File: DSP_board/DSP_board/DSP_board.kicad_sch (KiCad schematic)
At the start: 62 parts

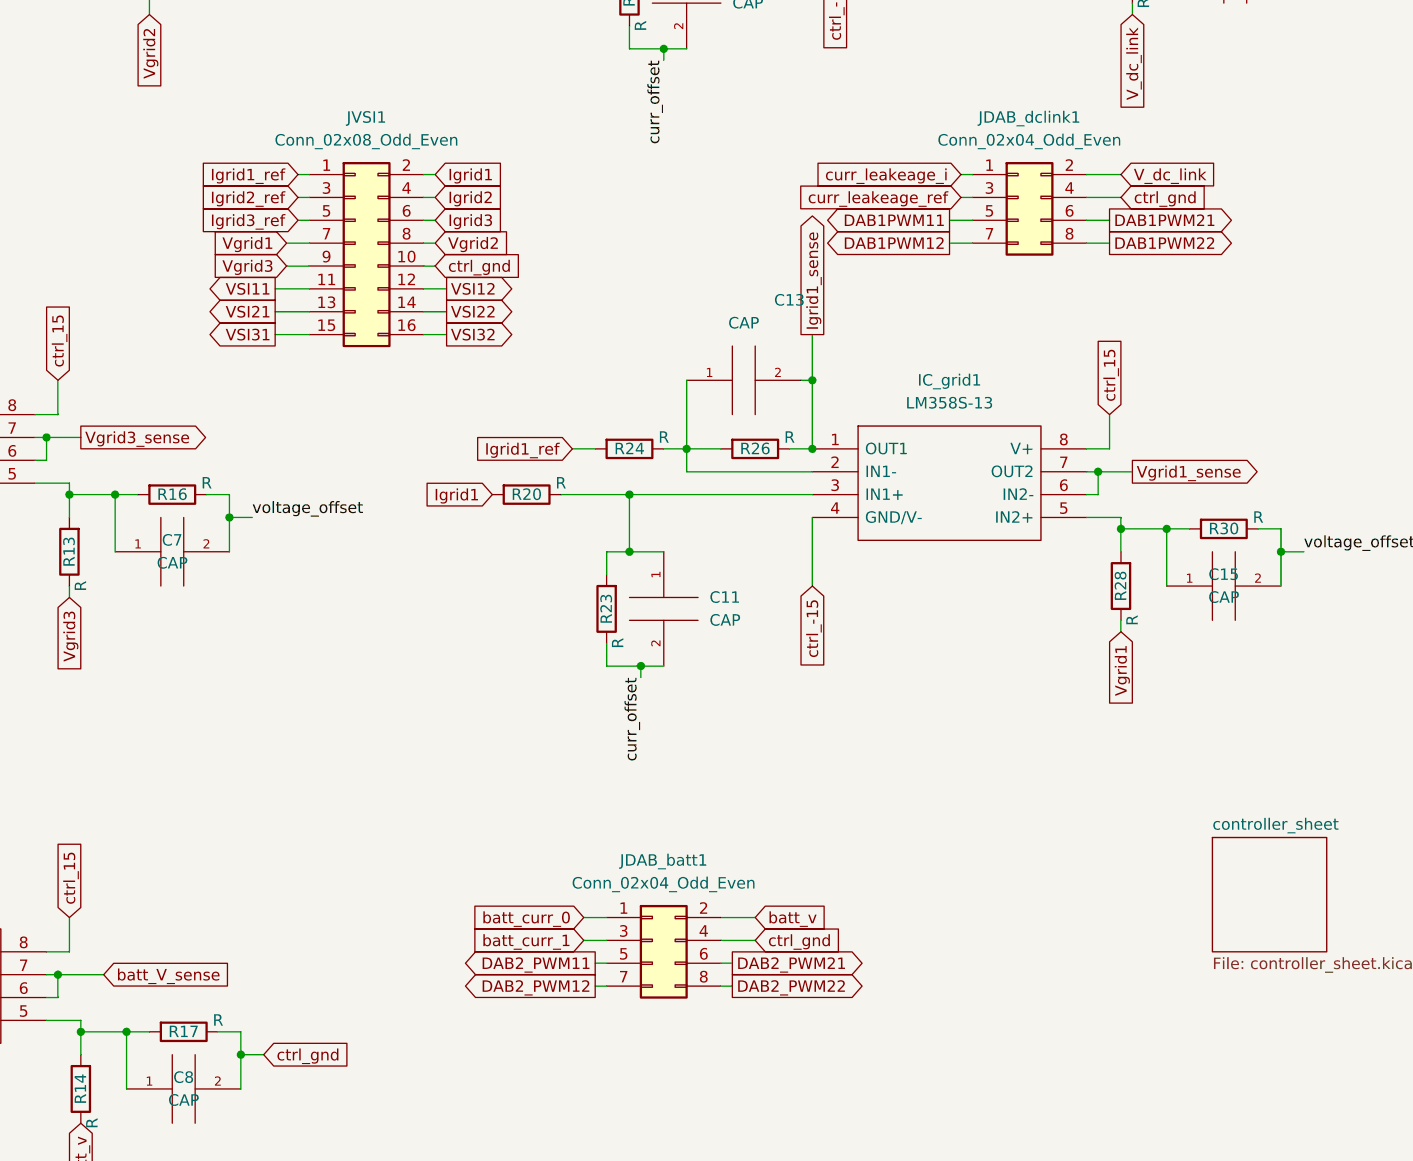
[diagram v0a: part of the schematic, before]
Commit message: including FPGA
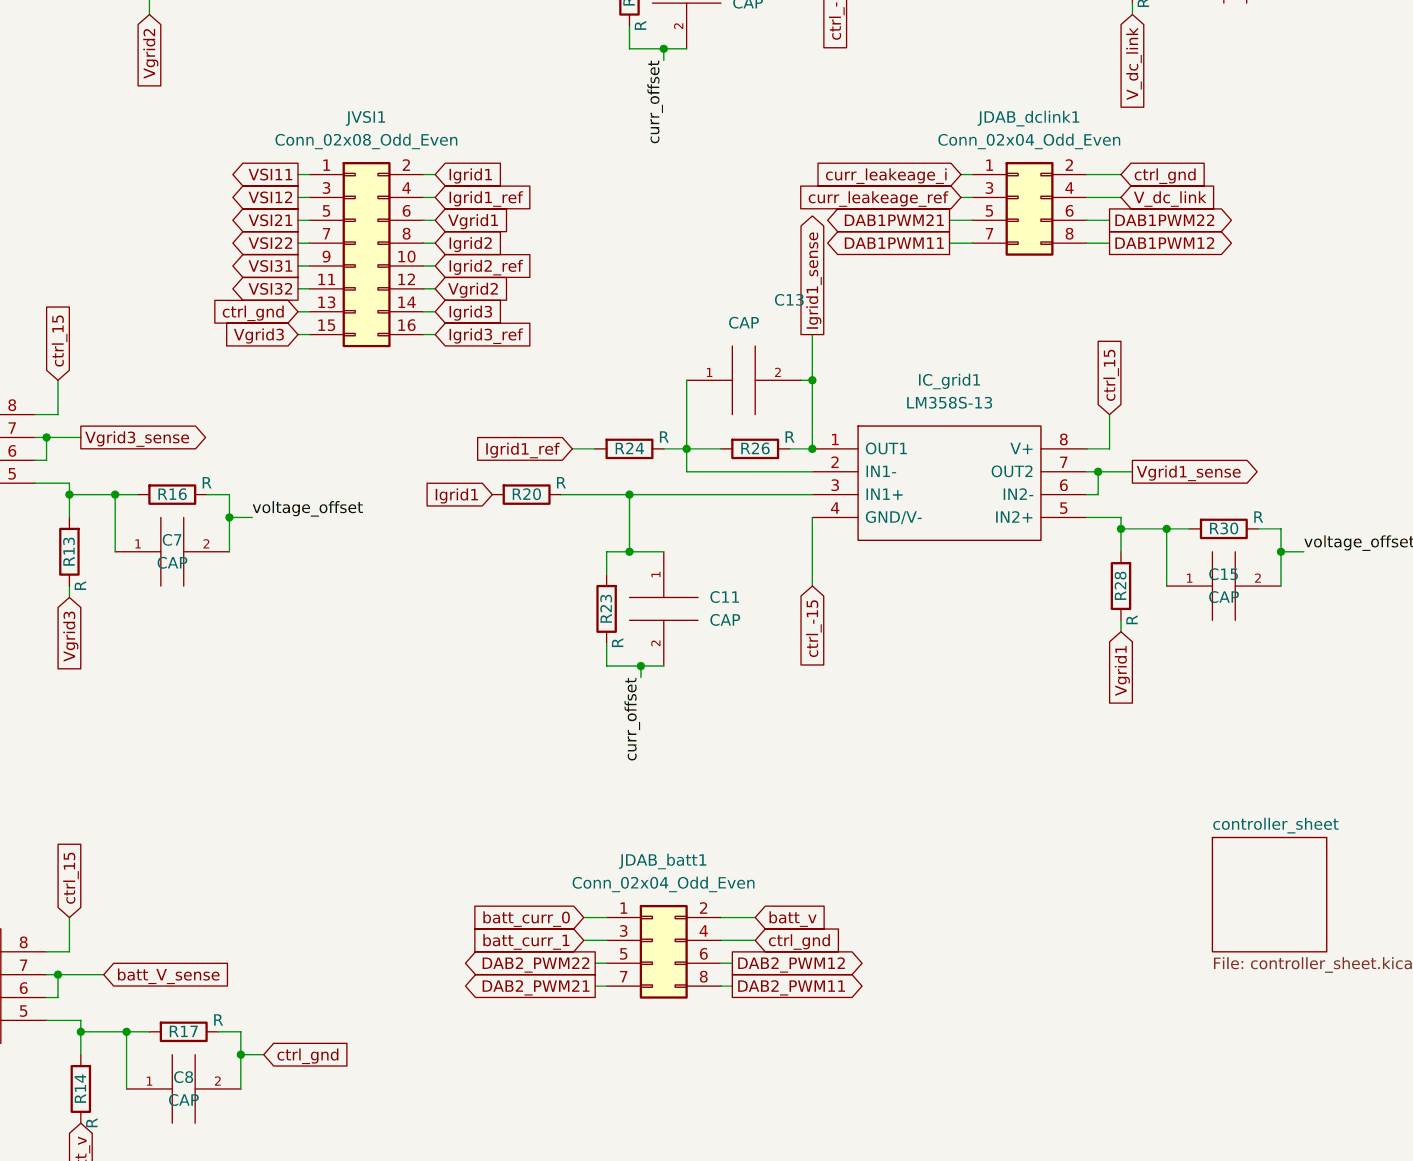
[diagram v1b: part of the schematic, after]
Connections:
- net DAB1PWM11: now also JDAB_dclink1.7 (Pin_7); no longer JDAB_dclink1.5 (Pin_5)
- net DAB1PWM12: now also JDAB_dclink1.8 (Pin_8); no longer JDAB_dclink1.7 (Pin_7)
- net DAB1PWM21: now also JDAB_dclink1.5 (Pin_5); no longer JDAB_dclink1.6 (Pin_6)
- net DAB1PWM22: now also JDAB_dclink1.6 (Pin_6); no longer JDAB_dclink1.8 (Pin_8)
- net DAB2_PWM11: now also JDAB_batt1.8 (Pin_8); no longer JDAB_batt1.5 (Pin_5)
- net DAB2_PWM12: now also JDAB_batt1.6 (Pin_6); no longer JDAB_batt1.7 (Pin_7)
- net DAB2_PWM21: now also JDAB_batt1.7 (Pin_7); no longer JDAB_batt1.6 (Pin_6)
- net DAB2_PWM22: now also JDAB_batt1.5 (Pin_5); no longer JDAB_batt1.8 (Pin_8)
- net Igrid1_ref: now also JVSI1.4 (Pin_4); no longer JVSI1.1 (Pin_1)
- net Igrid2: now also JVSI1.8 (Pin_8); no longer JVSI1.4 (Pin_4)
- net Igrid2_ref: now also JVSI1.10 (Pin_10); no longer JVSI1.3 (Pin_3)
- net Igrid3: now also JVSI1.14 (Pin_14); no longer JVSI1.6 (Pin_6)
- net Igrid3_ref: now also JVSI1.16 (Pin_16); no longer JVSI1.5 (Pin_5)
- net VSI11: now also JVSI1.1 (Pin_1); no longer JVSI1.11 (Pin_11)
- net VSI12: now also JVSI1.3 (Pin_3); no longer JVSI1.12 (Pin_12)
- net VSI21: now also JVSI1.5 (Pin_5); no longer JVSI1.13 (Pin_13)
- net VSI22: now also JVSI1.7 (Pin_7); no longer JVSI1.14 (Pin_14)
- net VSI31: now also JVSI1.9 (Pin_9); no longer JVSI1.15 (Pin_15)
- net VSI32: now also JVSI1.11 (Pin_11); no longer JVSI1.16 (Pin_16)
- net V_dc_link: now also JDAB_dclink1.4 (Pin_4); no longer JDAB_dclink1.2 (Pin_2)
- net Vgrid1: now also JVSI1.6 (Pin_6); no longer JVSI1.7 (Pin_7)
- net Vgrid2: now also JVSI1.12 (Pin_12); no longer JVSI1.8 (Pin_8)
- net Vgrid3: now also JVSI1.15 (Pin_15); no longer JVSI1.9 (Pin_9)
- net ctrl_gnd: now also JDAB_dclink1.2 (Pin_2), JVSI1.13 (Pin_13); no longer JDAB_dclink1.4 (Pin_4), JVSI1.10 (Pin_10)

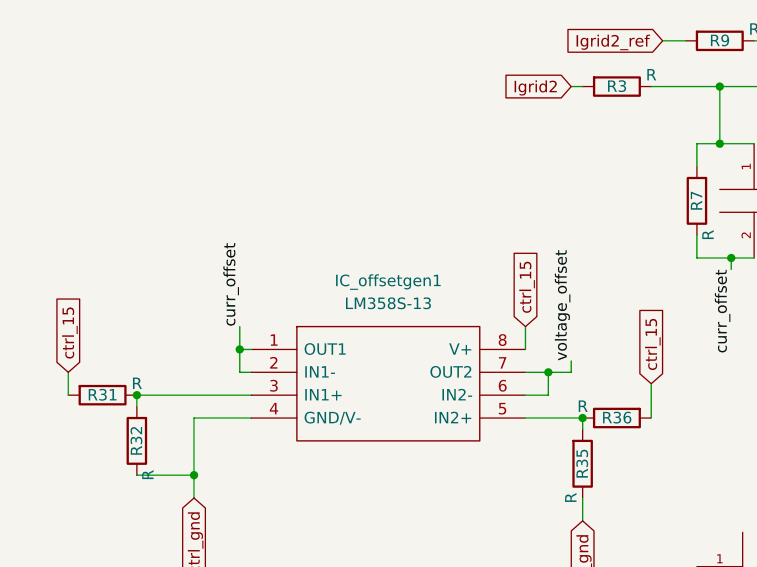
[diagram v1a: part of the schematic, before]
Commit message: Connecting FPGA ADC pins
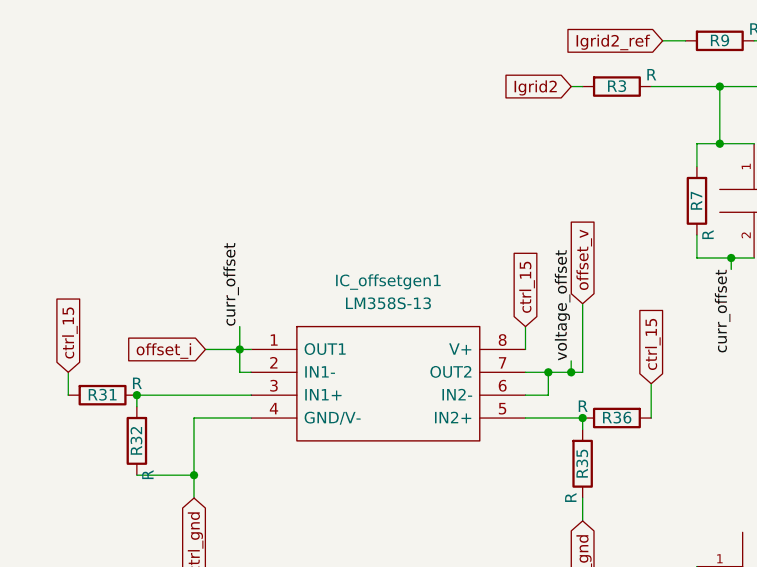
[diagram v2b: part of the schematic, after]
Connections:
- net curr_offset renamed offset_i
- net voltage_offset renamed offset_v
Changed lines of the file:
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@@
   (junction (at 27.94 129.54) (diameter 0) (color 0 0 0 0)
   )
+  (junction (at 72.39 69.85) (diameter 0) (color 0 0 0 0)
+  )
   (junction (at 34.29 138.43) (diameter 0) (color 0 0 0 0)
   )
@@
     (stroke (width 0) (type default) (color 0 0 0 0))
   )
+  (wire (pts (xy 31.75 67.31) (xy 35.56 67.31))
+    (stroke (width 0) (type default) (color 0 0 0 0))
+  )
   (wire (pts (xy 248.92 105.41) (xy 252.73 105.41))
     (stroke (width 0) (type default) (color 0 0 0 0))
@@
     (stroke (width 0) (type default) (color 0 0 0 0))
   )
+  (wire (pts (xy 73.66 62.23) (xy 73.66 69.85))
+    (stroke (width 0) (type default) (color 0 0 0 0))
+  )
   (wire (pts (xy 160.02 87.63) (xy 161.29 87.63))
     (stroke (width 0) (type default) (color 0 0 0 0))
@@
   )
   (wire (pts (xy 24.13 81.28) (xy 30.48 81.28))
+    (stroke (width 0) (type default) (color 0 0 0 0))
+  )
+  (wire (pts (xy 73.66 69.85) (xy 72.39 69.85))
     (stroke (width 0) (type default) (color 0 0 0 0))
   )
@@
     )
   )
+  (global_label "offset_v" (shape input) (at 73.66 62.23 90) (fields_autoplaced)
+    (effects (font (size 1.27 1.27)) (justify left))
+    (property "Intersheet References" "${INTERSHEET_REFS}" (id 0) (at 73.5806 52.4388 90)
+      (effects (font (size 1.27 1.27)) (justify left) hide)
+    )
+  )
   (global_label "batt_curr_sense" (shape input) (at 101.6 144.78 90) (fields_autoplaced)
     (effects (font (size 1.27 1.27)) (justify left))
@@
     (property "Intersheet References" "${INTERSHEET_REFS}" (id 0) (at 250.1106 21.4145 90)
       (effects (font (size 1.27 1.27)) (justify left) hide)
+    )
+  )
+  (global_label "offset_i" (shape input) (at 31.75 67.31 180) (fields_autoplaced)
+    (effects (font (size 1.27 1.27)) (justify right))
+    (property "Intersheet References" "${INTERSHEET_REFS}" (id 0) (at 22.3217 67.2306 0)
+      (effects (font (size 1.27 1.27)) (justify right) hide)
     )
   )
@@
       (reference "C18") (unit 1) (value "2.2u") (footprint "Capacitor_SMD:C_0603_1608Metric_Pad1.08x0.95mm_HandSolder")
     )
+    (path "/65abaeeb-f079-4d1a-9aaf-277d58cadcf0/9c5dc17f-dc69-4afc-8d49-ea02322f9d84"
+      (reference "C19") (unit 1) (value "C") (footprint "Capacitor_SMD:C_0805_2012Metric_Pad1.18x1.45mm_HandSolder")
+    )
     (path "/65abaeeb-f079-4d1a-9aaf-277d58cadcf0/e1c0c571-e1f3-4a66-88d8-43be5b9ae1e3"
       (reference "Cvdd_1") (unit 1) (value "0.1u") (footprint "Capacitor_SMD:C_0603_1608Metric_Pad1.08x0.95mm_HandSolder")
@@
       (reference "IC_offsetgen2") (unit 1) (value "LM358S-13") (footprint "SOIC127P600X175-8N")
     )
+    (path "/65abaeeb-f079-4d1a-9aaf-277d58cadcf0/692ebd42-656b-4507-a377-3238f0fabcc6"
+      (reference "J1") (unit 1) (value "Conn_01x02") (footprint "Connector_PinHeader_2.54mm:PinHeader_1x02_P2.54mm_Vertical")
+    )
+    (path "/65abaeeb-f079-4d1a-9aaf-277d58cadcf0/f918afd8-a761-444d-897a-d8a308105643"
+      (reference "J2") (unit 1) (value "Conn_01x02") (footprint "Connector_PinHeader_2.54mm:PinHeader_1x02_P2.54mm_Vertical")
+    )
+    (path "/65abaeeb-f079-4d1a-9aaf-277d58cadcf0/b83b5440-9edc-4017-a2d7-643658506b2b"
+      (reference "J3") (unit 1) (value "Conn_01x02") (footprint "Connector_PinHeader_2.54mm:PinHeader_1x02_P2.54mm_Vertical")
+    )
+    (path "/65abaeeb-f079-4d1a-9aaf-277d58cadcf0/12f56378-aad0-430d-8c18-21a9ea2b2532"
+      (reference "J4") (unit 1) (value "Conn_01x02") (footprint "Connector_PinHeader_2.54mm:PinHeader_1x02_P2.54mm_Vertical")
+    )
+    (path "/65abaeeb-f079-4d1a-9aaf-277d58cadcf0/1997d111-ebb0-4d66-b3d2-49f6e1d87919"
+      (reference "J5") (unit 1) (value "1-84981-0") (footprint "jtag_connector:1849810")
+    )
+    (path "/65abaeeb-f079-4d1a-9aaf-277d58cadcf0/9f0b94fc-42fa-421b-82bc-dd82d8110387"
+      (reference "J6") (unit 1) (value "Conn_01x02") (footprint "Connector_PinHeader_2.54mm:PinHeader_1x02_P2.54mm_Vertical")
+    )
     (path "/490c5d74-c269-42d2-9040-da4358a54472"
       (reference "JDAB_batt1") (unit 1) (value "Conn_02x04_Odd_Even") (footprint "Connector_PinSocket_2.54mm:PinSocket_2x04_P2.54mm_Vertical")
@@
       (reference "R36") (unit 1) (value "R") (footprint "Resistor_SMD:R_1206_3216Metric_Pad1.30x1.75mm_HandSolder")
     )
-  )
+    (path "/65abaeeb-f079-4d1a-9aaf-277d58cadcf0/80c9d4b5-88af-42a5-8108-1e39865f9764"
+      (reference "R37") (unit 1) (value "R") (footprint "Resistor_SMD:R_1206_3216Metric_Pad1.30x1.75mm_HandSolder")
+    )
+    (path "/65abaeeb-f079-4d1a-9aaf-277d58cadcf0/7988b86c-2205-4823-8413-bfb1980a92ea"
+      (reference "R38") (unit 1) (value "R") (footprint "Resistor_SMD:R_1206_3216Metric_Pad1.30x1.75mm_HandSolder")
+    )
+    (path "/65abaeeb-f079-4d1a-9aaf-277d58cadcf0/45d3761a-3cb6-4116-bda8-6f42efe8059d"
+      (reference "R39") (unit 1) (value "R") (footprint "Resistor_SMD:R_1206_3216Metric_Pad1.30x1.75mm_HandSolder")
+    )
+    (path "/65abaeeb-f079-4d1a-9aaf-277d58cadcf0/0984a727-41e6-41c4-a044-96da13a1e2c0"
+      (reference "R40") (unit 1) (value "R") (footprint "Resistor_SMD:R_1206_3216Metric_Pad1.30x1.75mm_HandSolder")
+    )
+    (path "/65abaeeb-f079-4d1a-9aaf-277d58cadcf0/24db0d00-bfd6-4645-8245-cc4b7c15fd71"
+      (reference "R41") (unit 1) (value "R") (footprint "Resistor_SMD:R_1206_3216Metric_Pad1.30x1.75mm_HandSolder")
+    )
+  )
